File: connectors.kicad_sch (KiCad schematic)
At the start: 8 parts, among them J1 Conn_01x02, J4 USB_C_Receptacle_USB2.0_14P

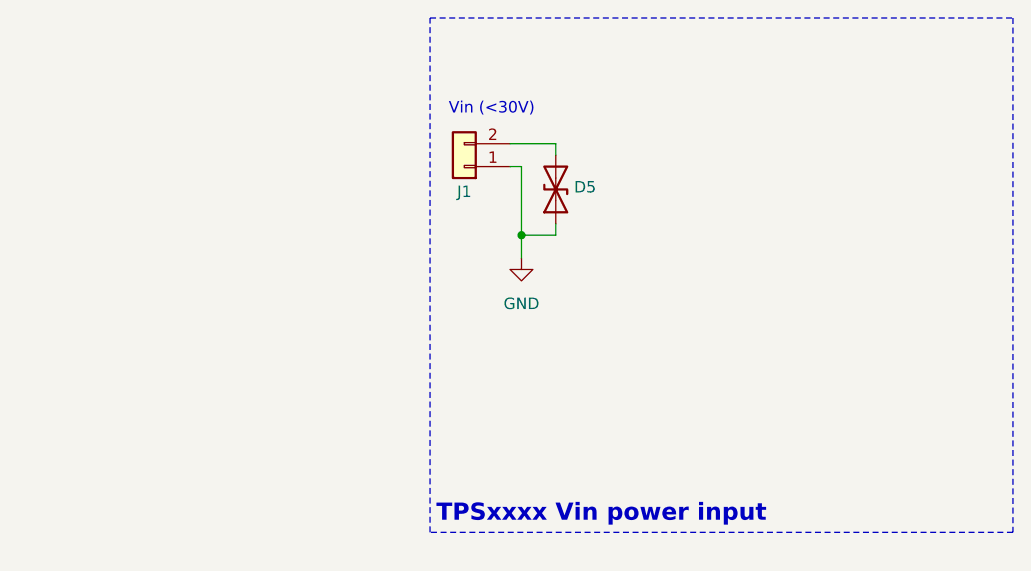
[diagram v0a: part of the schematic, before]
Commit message: symbol: update footprints library name
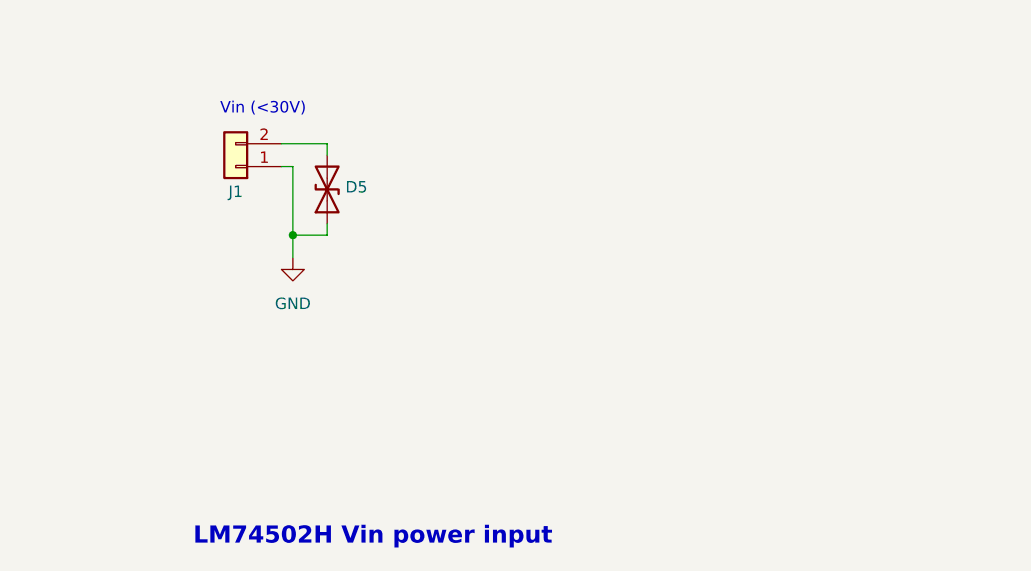
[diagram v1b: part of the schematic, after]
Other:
- note added: "LM74502H Vin power input"
- note removed: "TPSxxxx Vin power input"
- moved on the sheet: D5, J1
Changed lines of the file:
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@@
-		)
-	)
-	(rectangle
-		(start 186.69 72.39)
-		(end 251.46 129.54)
-		(stroke
-			(width 0)
-			(type dash)
-		)
-		(fill
-			(type none)
 		)
 	)
 	(text "Vin (<30V)"
 		(exclude_from_sim no)
-		(at 193.548 82.55 0)
+		(at 168.148 82.55 0)
 		(effects
 			(font
@@
 		)
 	)
-	(text "TPSxxxx Vin power input"
+	(text "LM74502H Vin power input"
 		(exclude_from_sim no)
-		(at 205.74 127.508 0)
+		(at 180.34 130.048 0)
 		(effects
 			(font
@@
 	)
 	(junction
-		(at 196.85 96.52)
+		(at 171.45 96.52)
 		(diameter 0)
 		(color 0 0 0 0)
@@
 	(wire
 		(pts
-			(xy 195.58 86.36) (xy 200.66 86.36)
+			(xy 170.18 86.36) (xy 175.26 86.36)
 		)
 		(stroke
@@
 	(wire
 		(pts
-			(xy 196.85 88.9) (xy 195.58 88.9)
-		)
-		(stroke
-			(width 0)
-			(type default)
-		)
-	)
-	(wire
-		(pts
-			(xy 200.66 95.25) (xy 200.66 96.52)
+			(xy 171.45 88.9) (xy 170.18 88.9)
+		)
+		(stroke
+			(width 0)
+			(type default)
+		)
+	)
+	(wire
+		(pts
+			(xy 175.26 95.25) (xy 175.26 96.52)
 		)
 		(stroke
@@
 	(wire
 		(pts
-			(xy 196.85 96.52) (xy 196.85 88.9)
+			(xy 171.45 96.52) (xy 171.45 88.9)
 		)
 		(stroke
@@
 	(wire
 		(pts
-			(xy 200.66 86.36) (xy 200.66 87.63)
-		)
-		(stroke
-			(width 0)
-			(type default)
-		)
-	)
-	(wire
-		(pts
-			(xy 200.66 96.52) (xy 196.85 96.52)
+			(xy 175.26 86.36) (xy 175.26 87.63)
+		)
+		(stroke
+			(width 0)
+			(type default)
+		)
+	)
+	(wire
+		(pts
+			(xy 175.26 96.52) (xy 171.45 96.52)
 		)
 		(stroke
@@
 	(wire
 		(pts
-			(xy 196.85 99.06) (xy 196.85 96.52)
+			(xy 171.45 99.06) (xy 171.45 96.52)
 		)
 		(stroke
@@
 	(symbol
 		(lib_id "Device:D_TVS")
-		(at 200.66 91.44 90)
+		(at 175.26 91.44 90)
 		(unit 1)
 		(exclude_from_sim no)
@@
 		(dnp no)
 		(property "Reference" "D5"
-			(at 202.692 91.186 90)
+			(at 177.292 91.186 90)
 			(effects
 				(font
@@
 		)
 		(property "Value" "D_TVS"
-			(at 203.2 92.7099 90)
+			(at 177.8 92.7099 90)
 			(effects
 				(font
@@
 		)
 		(property "Footprint" ""
-			(at 200.66 91.44 0)
+			(at 175.26 91.44 0)
 			(effects
 				(font
@@
 		)
 		(property "Datasheet" "~"
-			(at 200.66 91.44 0)
+			(at 175.26 91.44 0)
 			(effects
 				(font
@@
 		)
 		(property "Description" "Bidirectional transient-voltage-suppression diode"
-			(at 200.66 91.44 0)
+			(at 175.26 91.44 0)
 			(effects
 				(font
@@
 	(symbol
 		(lib_id "Connector_Generic:Conn_01x02")
-		(at 190.5 88.9 180)
+		(at 165.1 88.9 180)
 		(unit 1)
 		(exclude_from_sim no)
@@
 		(dnp no)
 		(property "Reference" "J1"
-			(at 190.5 91.694 0)
+			(at 165.1 91.694 0)
 			(effects
 				(font
@@
 		)
 		(property "Value" "Conn_01x02"
-			(at 190.5 82.55 0)
+			(at 165.1 82.55 0)
 			(effects
 				(font
@@
 		)
 		(property "Footprint" ""
-			(at 190.5 88.9 0)
+			(at 165.1 88.9 0)
 			(effects
 				(font
@@
 		)
 		(property "Datasheet" "~"
-			(at 190.5 88.9 0)
+			(at 165.1 88.9 0)
 			(effects
 				(font
@@
 		)
 		(property "Description" "Generic connector, single row, 01x02, script generated (kicad-library-utils/schlib/autogen/connector/)"
-			(at 190.5 88.9 0)
+			(at 165.1 88.9 0)
 			(effects
 				(font
@@
 	(symbol
 		(lib_id "power:GND")
-		(at 196.85 99.06 0)
+		(at 171.45 99.06 0)
 		(unit 1)
 		(exclude_from_sim no)
@@
 		(fields_autoplaced yes)
 		(property "Reference" "#PWR044"
-			(at 196.85 105.41 0)
+			(at 171.45 105.41 0)
 			(effects
 				(font
@@
 		)
 		(property "Value" "GND"
-			(at 196.85 104.14 0)
+			(at 171.45 104.14 0)
 			(effects
 				(font
@@
 		)
 		(property "Footprint" ""
-			(at 196.85 99.06 0)
+			(at 171.45 99.06 0)
 			(effects
 				(font
@@
 		)
 		(property "Datasheet" ""
-			(at 196.85 99.06 0)
+			(at 171.45 99.06 0)
 			(effects
 				(font
@@
 		)
 		(property "Description" "Power symbol creates a global label with name \"GND\" , ground"
-			(at 196.85 99.06 0)
-			(effects
-				(font
+			(at 171.45 99.06 0)
+			(effects
+				(font

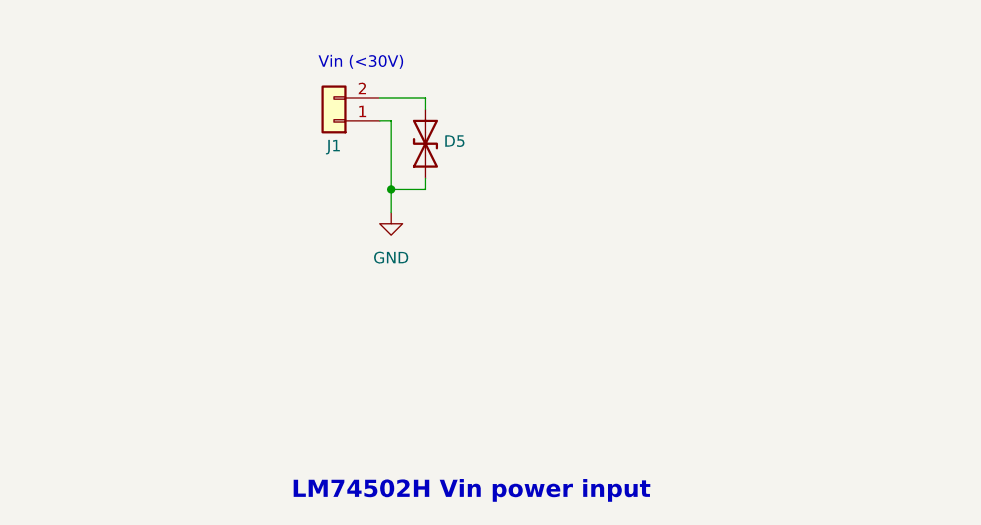
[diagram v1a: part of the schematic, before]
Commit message: schem: add LM74502H Vin power input
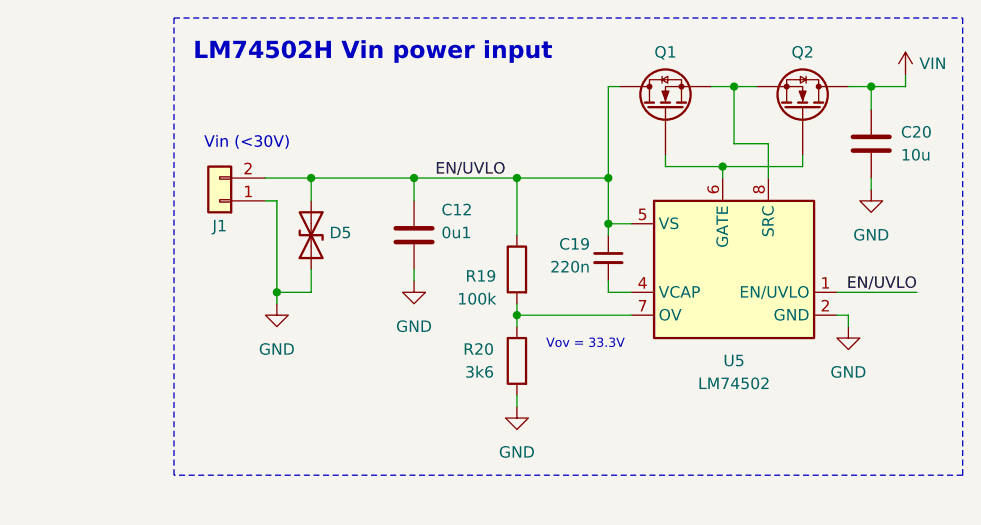
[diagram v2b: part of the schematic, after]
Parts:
- added C12: 0u1, symbol Device:C
- added C19: 220n, symbol Device:C_Small
- added C20: 10u, symbol Device:C
- added Q1, Q2: Q_NMOS, symbol Device:Q_NMOS
- added R19: 100k, symbol Device:R
- added R20: 3k6, symbol Device:R
- added U5: LM74502, GLCS:SOT-23-8, symbol GLCS:LM74502
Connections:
- net GND: now also C12.2, C20.2, R20.2, U5.2 (GND)
- net EN/UVLO: now reaches D5.2 (A2), J1.2 (Pin_2)
- net EN/UVLO: now also C12.1, C19.1, Q1.D, R19.1, U5.1 (EN/UVLO), U5.5 (VS)
- new net: Q1.G, Q2.G, U5.6 (GATE)
- new net: Q1.S, Q2.S, U5.8 (SRC)
- new net: C19.2, U5.4 (VCAP)
- new net: R19.2, R20.1, U5.7 (OV)
- new net VIN: C20.1, Q2.D
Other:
- note added: "Vov = 33.3V"
- moved on the sheet: D5, J1

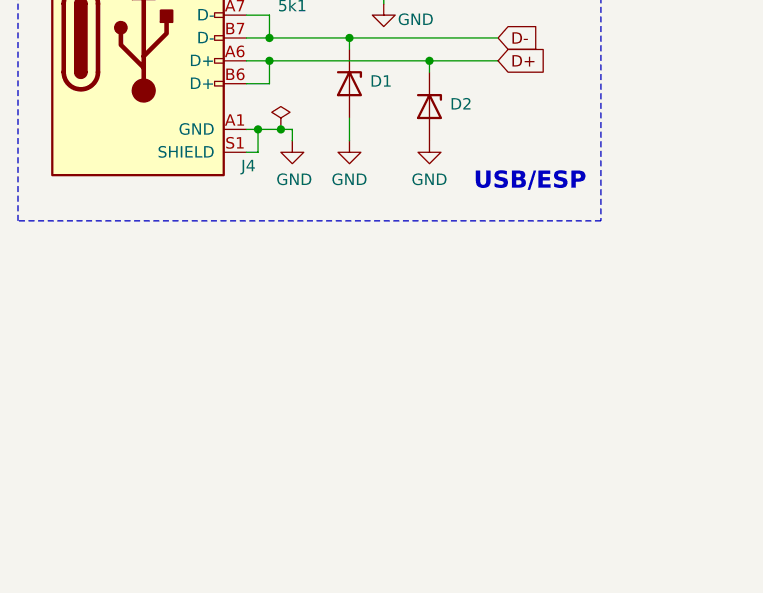
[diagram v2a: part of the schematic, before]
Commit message: schem: add servos connectors
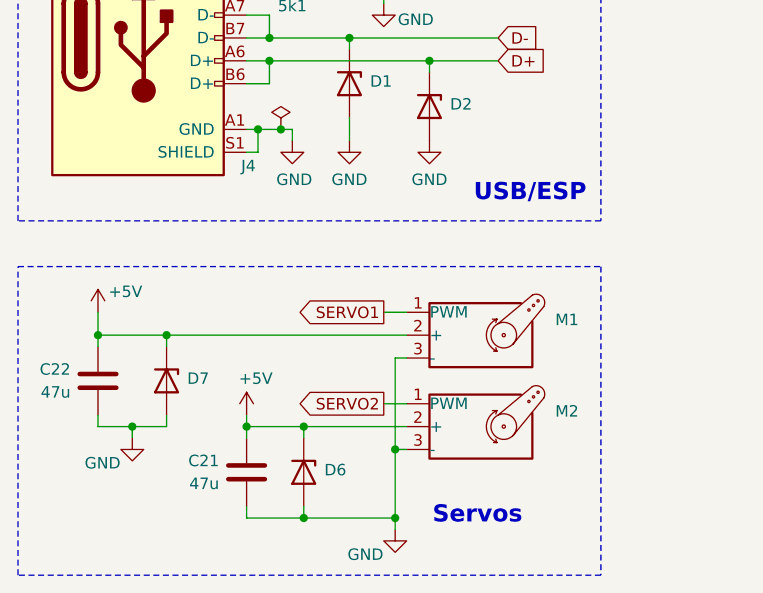
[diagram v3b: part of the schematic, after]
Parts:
- added C21, C22: 47u, symbol Device:C
- added D6, D7: H5VU10U, Pers:Diode_DFN1006, symbol Pers:H5VU10U
- added M1, M2: Motor_Servo, symbol Motor:Motor_Servo
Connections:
- net GND: now also C21.2, C22.2, D6.2 (A), D7.2 (A), M1.3 (-), M2.3 (-)
- new net +5V: C21.1, C22.1, D6.1 (K), D7.1 (K), M1.2 (+), M2.2 (+)
- new net SERVO1: M1.1 (PWM)
- new net SERVO2: M2.1 (PWM)
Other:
- note added: "Servos"

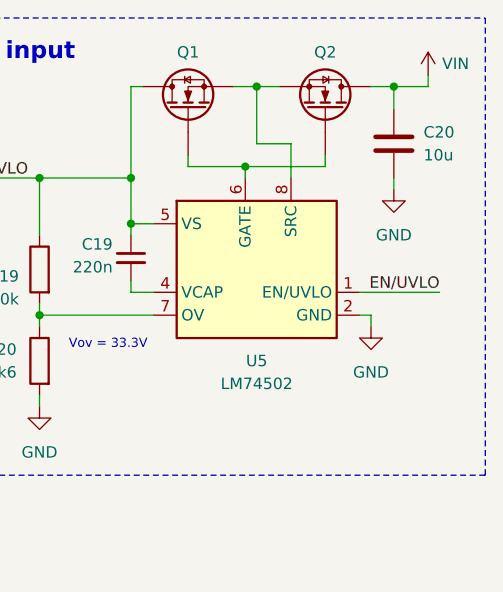
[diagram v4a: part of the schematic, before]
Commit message: schem: add LM74502H enable jumper
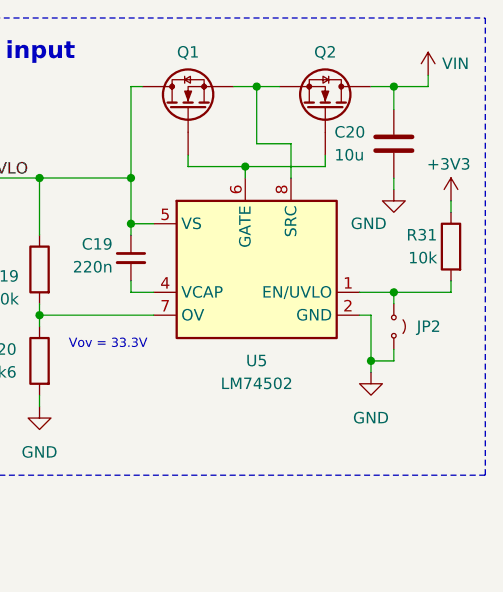
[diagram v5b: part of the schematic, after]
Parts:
- added JP2: Jumper_2_Small_Open, symbol Jumper:Jumper_2_Small_Open
- added R31: 10k, symbol Device:R
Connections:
- net EN/UVLO: no longer U5.1 (EN/UVLO)
- net GND: now also JP2.2 (B)
- new net: JP2.1 (A), R31.2, U5.1 (EN/UVLO)
- new net +3V3: R31.1

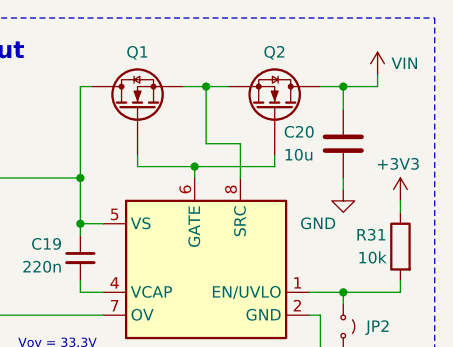
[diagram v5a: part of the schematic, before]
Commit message: schem: add Vin driver input selection circuit
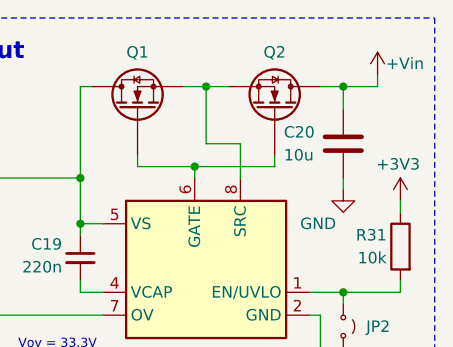
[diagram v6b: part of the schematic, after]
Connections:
- net VIN renamed +Vin
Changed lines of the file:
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@@
 			)
 		)
-		(property "Value" "VIN"
+		(property "Value" "+Vin"
 			(at 231.648 82.55 0)
 			(effects

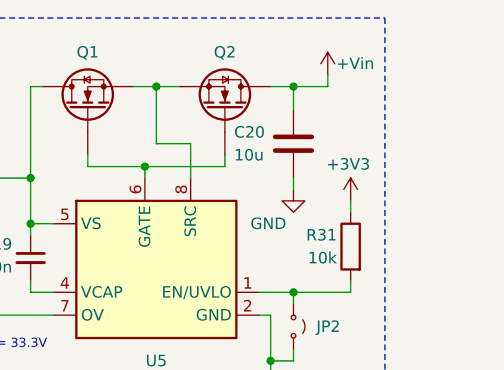
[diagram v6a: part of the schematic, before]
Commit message: schem: add pins to hierachical sheets
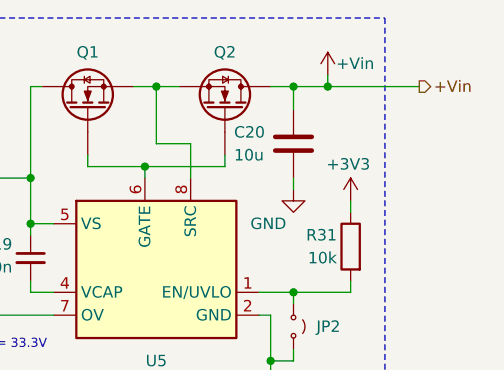
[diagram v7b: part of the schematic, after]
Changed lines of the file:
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@@
+	)
+	(junction
+		(at 228.6 85.09)
+		(diameter 0)
+		(color 0 0 0 0)
 	)
 	(junction
@@
 		(pts
 			(xy 195.58 100.33) (xy 195.58 101.6)
+		)
+		(stroke
+			(width 0)
+			(type default)
+		)
+	)
+	(wire
+		(pts
+			(xy 228.6 85.09) (xy 238.76 85.09)
 		)
 		(stroke
@@
 		)
 	)
+	(hierarchical_label "+Vin"
+		(shape output)
+		(at 238.76 85.09 0)
+		(effects
+			(font
+				(size 1.27 1.27)
+			)
+			(justify left)
+		)
+	)

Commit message: schem: add +Vbus to hierachical
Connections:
- net VBUS renamed +Vbus
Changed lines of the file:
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@@
 	)
 	(junction
+		(at 107.95 88.9)
+		(diameter 0)
+		(color 0 0 0 0)
+	)
+	(junction
 		(at 222.25 115.57)
 		(diameter 0)
@@
 	(wire
 		(pts
+			(xy 107.95 88.9) (xy 111.76 88.9)
+		)
+		(stroke
+			(width 0)
+			(type default)
+		)
+	)
+	(wire
+		(pts
 			(xy 88.9 114.3) (xy 91.44 114.3)
 		)
@@
 		)
 	)
+	(hierarchical_label "+Vbus"
+		(shape output)
+		(at 111.76 88.9 0)
+		(effects
+			(font
+				(size 1.27 1.27)
+			)
+			(justify left)
+		)
+	)
 	(hierarchical_label "+Vin"
 		(shape output)
@@
 			)
 		)
-		(property "Value" "VBUS"
-			(at 110.49 85.852 0)
+		(property "Value" "+Vbus"
+			(at 99.822 84.582 0)
 			(effects
 				(font
